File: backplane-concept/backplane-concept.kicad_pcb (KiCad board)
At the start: 2 copper layers, 60 x 91.8 mm, 2 parts

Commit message: Backplane Ideas
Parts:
- added J3: PCIE_8x_Labeled, !footprints:9-1734774-5, F.Cu at (60.0, 60.0)
- added J4: PCIE_8x_Labeled, !footprints:9-1734774-5, F.Cu at (60.0, 40.0)
- added J5: CONN_MINI, !footprints:10018784-10200TLF, F.Cu at (60.0, 100.0)
- added J6: CONN_MINI, !footprints:10018784-10200TLF, F.Cu at (60.0, 120.0)
- added J7: CONN_MINI, !footprints:10018784-10200TLF, F.Cu at (60.0, 140.0)
- added J8: CONN_MINI, !footprints:10018784-10200TLF, F.Cu at (60.0, 160.0)
- added U1: PRIMARY, !footprints:SPARKFUN_SEN-13879, F.Cu at (130.0, 83.0)
- added U2: SECONDARY, !footprints:SPARKFUN_SEN-13879, F.Cu at (130.0, 59.0)
- added U3: NAU7802SGI, !footprints:NAU7802SGI, F.Cu at (122.0, 100.0)
- added U5: ESP32-PICO-D4, Package_DFN_QFN:QFN-48-1EP_7x7mm_P0.5mm_EP5.3x5.3mm, F.Cu at (98.7, 161.7)
- J1: value ~ -> 6473427-1; footprint !footprints:9-1734774-5 -> !footprints:64734271
- J2: value ~ -> PCIE_8x_Labeled
- moved J1 112.2 mm to (117.2, 163.2), turned to 90 degrees
- moved J2 43.7 mm to (60.0, 80.0)
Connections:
- J1 pad A1: 5V -> +5V
- J1 pad A10: GND -> +5V
- J1 pad A11: GND -> ENCA_P
- J1 pad A12: ENGHALL1 -> ~ENCA_P
- J1 pad A13: DIR2 -> ENCB_P
- J1 pad A14: DIR1 -> ~ENCB_P
- J1 pad A15: PWM2 -> ENCI_P
- J1 pad A16: PWM1 -> ~ENCI_P
- J1 pad A18: SPARK -> +5V
- J1 pad A19: RRHALL -> ENCA_S
- J1 pad A2: 5V -> HALL1_P
- J1 pad A20: ENGHALL2 -> ~ENCA_S
- J1 pad A21: GND -> ENCB_S
- J1 pad A22: PLOADC1 -> ~ENCB_S
- J1 pad A23: PLOADC2 -> ENCI_S
- J1 pad A24: PLDCLK -> ~ENCI_S
- J1 pad A25: PLDDAT -> GND
- J1 pad A26: SLOADC1 -> +5V
- J1 pad A27: SLOADC2 -> HALL1_S
- J1 pad A28: SLDCLK -> HALL2_S
- J1 pad A29: SLDDAT -> HALL3_S
- J1 pad A3: 5V -> HALL2_P
- J1 pad A30: PENC_A -> GND
- J1 pad A31: ~PENC_A -> THERM_S
- J1 pad A32: PENC_B -> MOT1_S
- J1 pad A33: ~PENC_B -> MOT2_S
- J1 pad A34: SENC_A -> MOT3_S
- J1 pad A4: 3.3V -> HALL3_P
- J1 pad A5: 3.3V -> GND
- J1 pad A6: 3.3V -> THERM_P
- J1 pad A7: 8.4V -> MOT1_P
- J1 pad A8: 8.4V -> MOT2_P
- J1 pad A9: GND -> MOT3_P
- J1 pad B1: 5V -> GND
- J1 pad B10: GND -> +3V3
- J1 pad B12: CAN_H -> GND
- J1 pad B13: CAN_L -> THERM_A1_CASE
- J1 pad B14: GND -> THERM_A2_CASE
- J1 pad B15: I2C_DATA -> GND
- J1 pad B16: I2C_CLK -> IN+_P
- J1 pad B17: GND -> IN-_P
- J1 pad B18: TX1 -> AVDD_S
- J1 pad B19: RX1 -> GND
- J1 pad B2: 5V -> GND
- J1 pad B20: TX2 -> IN+_S
- J1 pad B21: RX2 -> IN-_S
- J1 pad B22: TX3 -> AVDD_S
- J1 pad B23: RX3 -> GND
- J1 pad B24: TX4 -> GND
- J1 pad B25: RX4 -> +3V3
- J1 pad B26: TX5 -> +3V3
- J1 pad B3: 5V -> HALL_ENG1
- J1 pad B4: 3.3V -> HALL_ENG2
- J1 pad B5: 3.3V -> +8V
- J1 pad B6: 3.3V -> +8V
- J1 pad B7: 8.4V -> GND
- J1 pad B8: 8.4V -> I2C1_ECVT_EXT_SDA
- J1 pad B9: GND -> I2C1_ECVT_EXT_SCL
- J2 pad A1: 5V -> +5V
- J2 pad A12: ENGHALL1 -> DAQ_TX0_ECVT_RX0
- J2 pad A13: DIR2 -> DAQ_RX0_ECVT_TX0
- J2 pad A14: DIR1 -> DAQ_TX1_DATA
- J2 pad A15: PWM2 -> GND
- J2 pad A16: PWM1 -> I2C1_DAQ_SDA
- J2 pad A17: GND -> I2C1_DAQ_SCL
- J2 pad A18: SPARK -> GND
- J2 pad A19: RRHALL -> unconnected-(J2-PadA19)
- J2 pad A2: 5V -> +5V
- J2 pad A20: ENGHALL2 -> unconnected-(J2-PadA20)
- J2 pad A21: GND -> unconnected-(J2-PadA21)
- J2 pad A22: PLOADC1 -> unconnected-(J2-PadA22)
- J2 pad A23: PLOADC2 -> unconnected-(J2-PadA23)
- J2 pad A24: PLDCLK -> unconnected-(J2-PadA24)
- J2 pad A25: PLDDAT -> unconnected-(J2-PadA25)
- J2 pad A26: SLOADC1 -> unconnected-(J2-PadA26)
- J2 pad A27: SLOADC2 -> unconnected-(J2-PadA27)
- J2 pad A28: SLDCLK -> GND
- J2 pad A29: SLDDAT -> ENCA_P
- J2 pad A3: 5V -> +5V
- J2 pad A30: PENC_A -> ~ENCA_P
- J2 pad A31: ~PENC_A -> ENCB_P
- J2 pad A32: PENC_B -> ~ENCB_P
- J2 pad A33: ~PENC_B -> ENCI_P
- J2 pad A34: SENC_A -> ~ENCI_P
- J2 pad A35: ~SENC_A -> GND
- J2 pad A36: SENC_B -> ENCA_S
- J2 pad A37: ~SENC_B -> ~ENCA_S
- J2 pad A38: GND -> ENCB_S
- J2 pad A39: DIG_OUT -> ~ENCB_S
- J2 pad A4: 3.3V -> +3V3
- J2 pad A40: N_A -> ENCI_S
- J2 pad A41: IR_TEENSY -> ~ENCI_S
- J2 pad A42: IR_AMP -> SPARK
- J2 pad A43: unconnected-(J2-PadA43) -> GND
- J2 pad A44: unconnected-(J2-PadA44) -> THERM_P
- J2 pad A45: GND -> THERM_S
- J2 pad A46: TEMP4 -> THERM_A1_CASE
- J2 pad A47: TEMP3 -> THERM_A2_CASE
- J2 pad A48: TEMP2 -> THERM_A3
- J2 pad A49: TEMP1 -> THERM_A4
- J2 pad A5: 3.3V -> +3V3
- J2 pad A6: 3.3V -> +3V3
- J2 pad A7: 8.4V -> +8V
- J2 pad A8: 8.4V -> +8V
- J2 pad B1: 5V -> +5V
- J2 pad B14: GND -> I2C0_DAQ_SDA
- J2 pad B15: I2C_DATA -> I2C0_DAQ_SCL
- J2 pad B16: I2C_CLK -> I2C0_ECVT_SDA
- J2 pad B17: GND -> I2C0_ECVT_SCL
- J2 pad B18: TX1 -> GND
- J2 pad B19: RX1 -> unconnected-(J2-PadB19)
- J2 pad B2: 5V -> +5V
- J2 pad B20: TX2 -> unconnected-(J2-PadB20)
- J2 pad B21: RX2 -> unconnected-(J2-PadB21)
- J2 pad B22: TX3 -> unconnected-(J2-PadB22)
- J2 pad B23: RX3 -> unconnected-(J2-PadB23)
- J2 pad B24: TX4 -> unconnected-(J2-PadB24)
- J2 pad B25: RX4 -> unconnected-(J2-PadB25)
- J2 pad B26: TX5 -> unconnected-(J2-PadB26)
- J2 pad B27: RX5 -> unconnected-(J2-PadB27)
- J2 pad B28: GND -> LOADC_CLK_P
- J2 pad B29: CIPO -> LOADC_DAT_P
- J2 pad B3: 5V -> +5V
- J2 pad B30: COPI -> LOADC_CLK_P
- J2 pad B31: SCLK -> LOADC_DAT_S
- J2 pad B32: CS1 -> GND
- J2 pad B33: CS2 -> HALL_ENG1
- J2 pad B34: CS3 -> HALL_RW
- J2 pad B35: CS4 -> PWM_P
- J2 pad B36: CS5 -> DIR_P
- J2 pad B37: CS6 -> PWM_S
- J2 pad B38: unconnected-(J2-PadB38) -> DIR_S
- J2 pad B39: unconnected-(J2-PadB39) -> I2C1_ECVT_EXT_SDA
- J2 pad B4: 3.3V -> +3V3
- J2 pad B40: unconnected-(J2-PadB40) -> I2C1_ECVT_EXT_SCL
- J2 pad B41: unconnected-(J2-PadB41) -> HALL_ENG2
- J2 pad B43: FRBPRESS -> GND
- J2 pad B44: RRBPRESS -> BP_FRONT
- J2 pad B45: RPOT1 -> BP_REAR
- J2 pad B46: RPOT2 -> RPOT1
- J2 pad B47: VOLT1 -> RPOT2
- J2 pad B48: VOLT2 -> Net-(J2-PadB48)
- J2 pad B49: VOLT3 -> Net-(J2-PadB49)
- J2 pad B5: 3.3V -> +3V3
- J2 pad B6: 3.3V -> +3V3
- J2 pad B7: 8.4V -> +8V
- J2 pad B8: 8.4V -> +8V
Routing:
- net GND: track 166.5 -> 452.8 mm, vias 0 -> 16
- net I2C0_ECVT_SCL: track 0.00 -> 127.0 mm, vias 0 -> 12
- net I2C0_DAQ_SCL: track 0.00 -> 127.0 mm, vias 0 -> 12
- net I2C0_ECVT_SDA: track 0.00 -> 123.8 mm, vias 0 -> 12
- net I2C0_DAQ_SDA: track 0.00 -> 123.8 mm, vias 0 -> 12
- net DAQ_RX0_ECVT_TX0: track 0.00 -> 122.8 mm
- net I2C1_DAQ_SCL: track 0.00 -> 122.8 mm
- net I2C1_DAQ_SDA: track 0.00 -> 122.7 mm
- net DAQ_TX1_DATA: track 0.00 -> 122.7 mm
- net DAQ_TX0_ECVT_RX0: track 0.00 -> 122.7 mm
- net LOADC_CLK_P: track 0.00 -> 82.5 mm, vias 0 -> 8
- net CAN_L: track 62.0 -> 127.0 mm, vias 0 -> 12
- net CAN_H: track 62.0 -> 123.8 mm, vias 0 -> 12
- net PWM_P: track 0.00 -> 42.5 mm, vias 0 -> 4
- net LOADC_DAT_S: track 0.00 -> 42.5 mm, vias 0 -> 4
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- added copper zone on B.Cu, net +3V3
- added copper zone on F.Cu, net +3V3
- added copper zone on B.Cu, net +5V
- added copper zone on F.Cu, net +5V
- added copper zone on B.Cu, net +8V
- added copper zone on F.Cu, net +8V
- removed copper zone on B.Cu, net 3.3V
- removed copper zone on F.Cu, net 3.3V
- removed copper zone on B.Cu, net 5V
- removed copper zone on F.Cu, net 5V
- removed copper zone on B.Cu, net 8.4V
- removed copper zone on F.Cu, net 8.4V
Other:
- board size 60 x 91.8 mm -> 90 x 140 mm

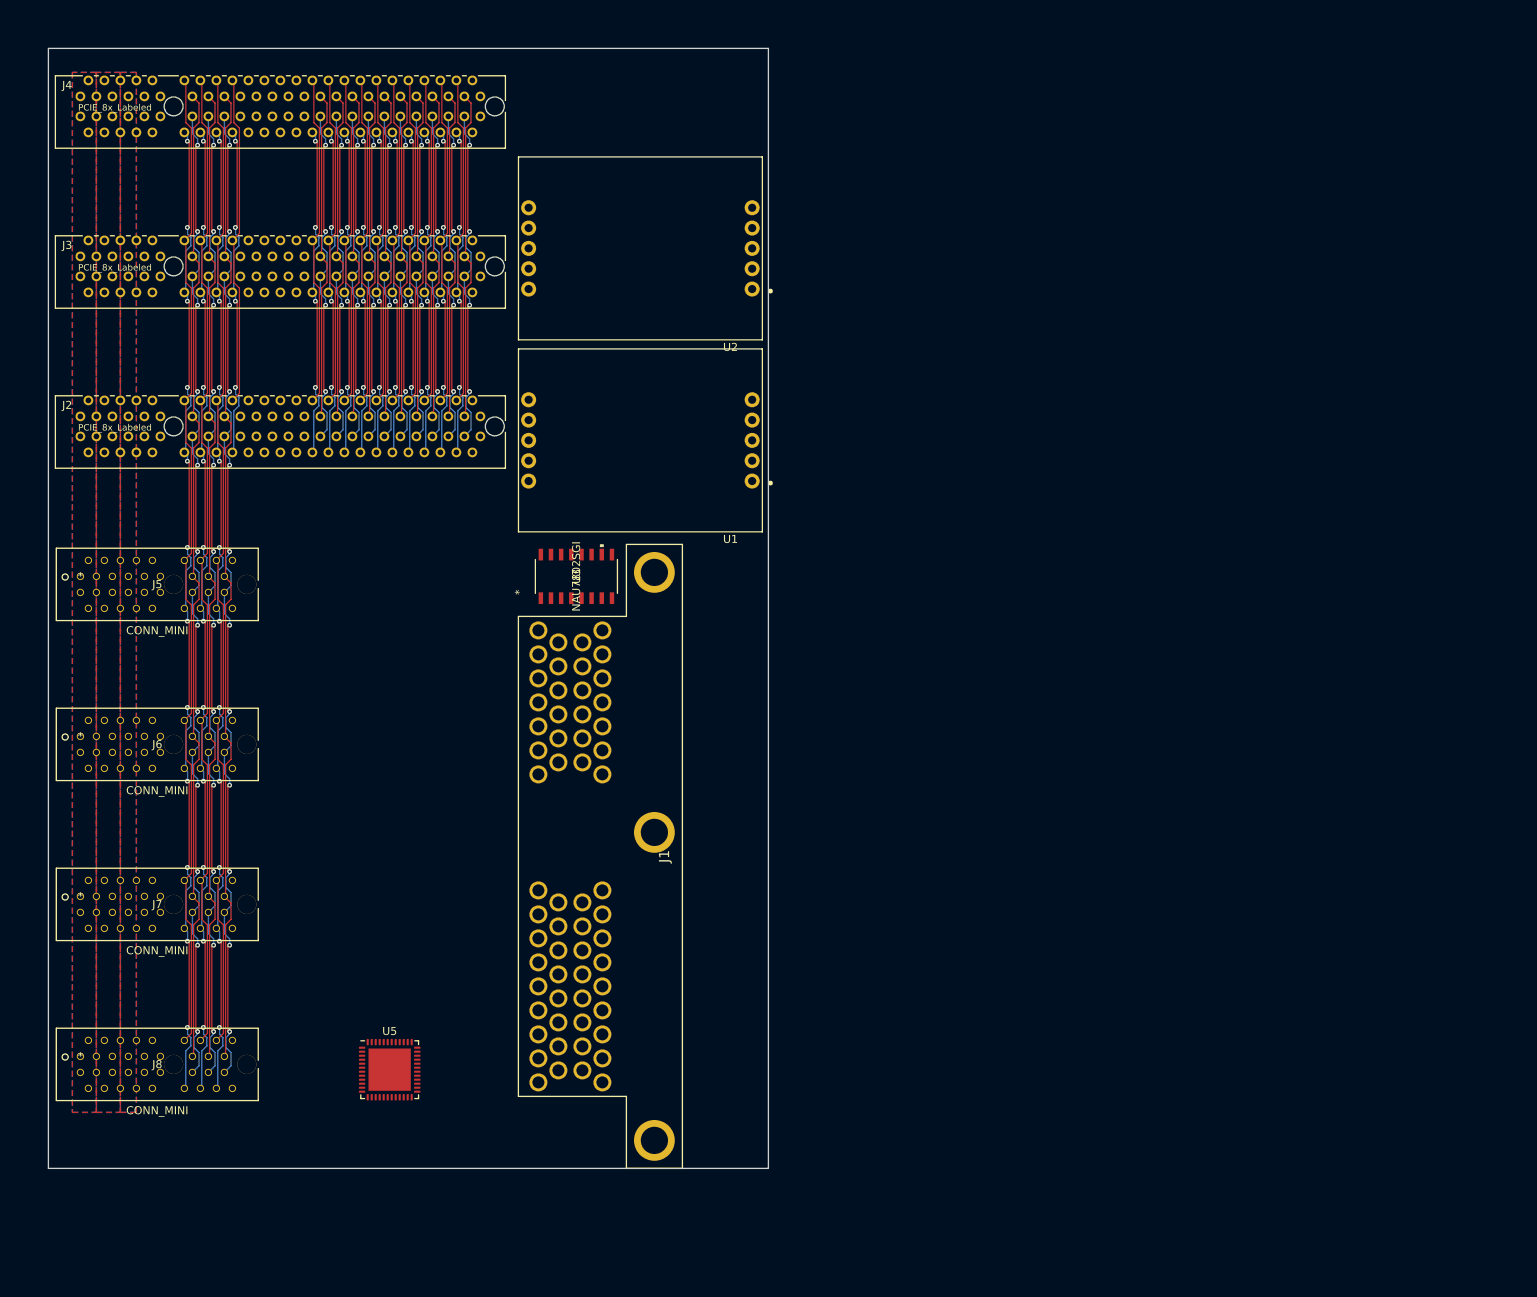
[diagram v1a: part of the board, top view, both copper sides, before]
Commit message: Design PSUs, route bucks
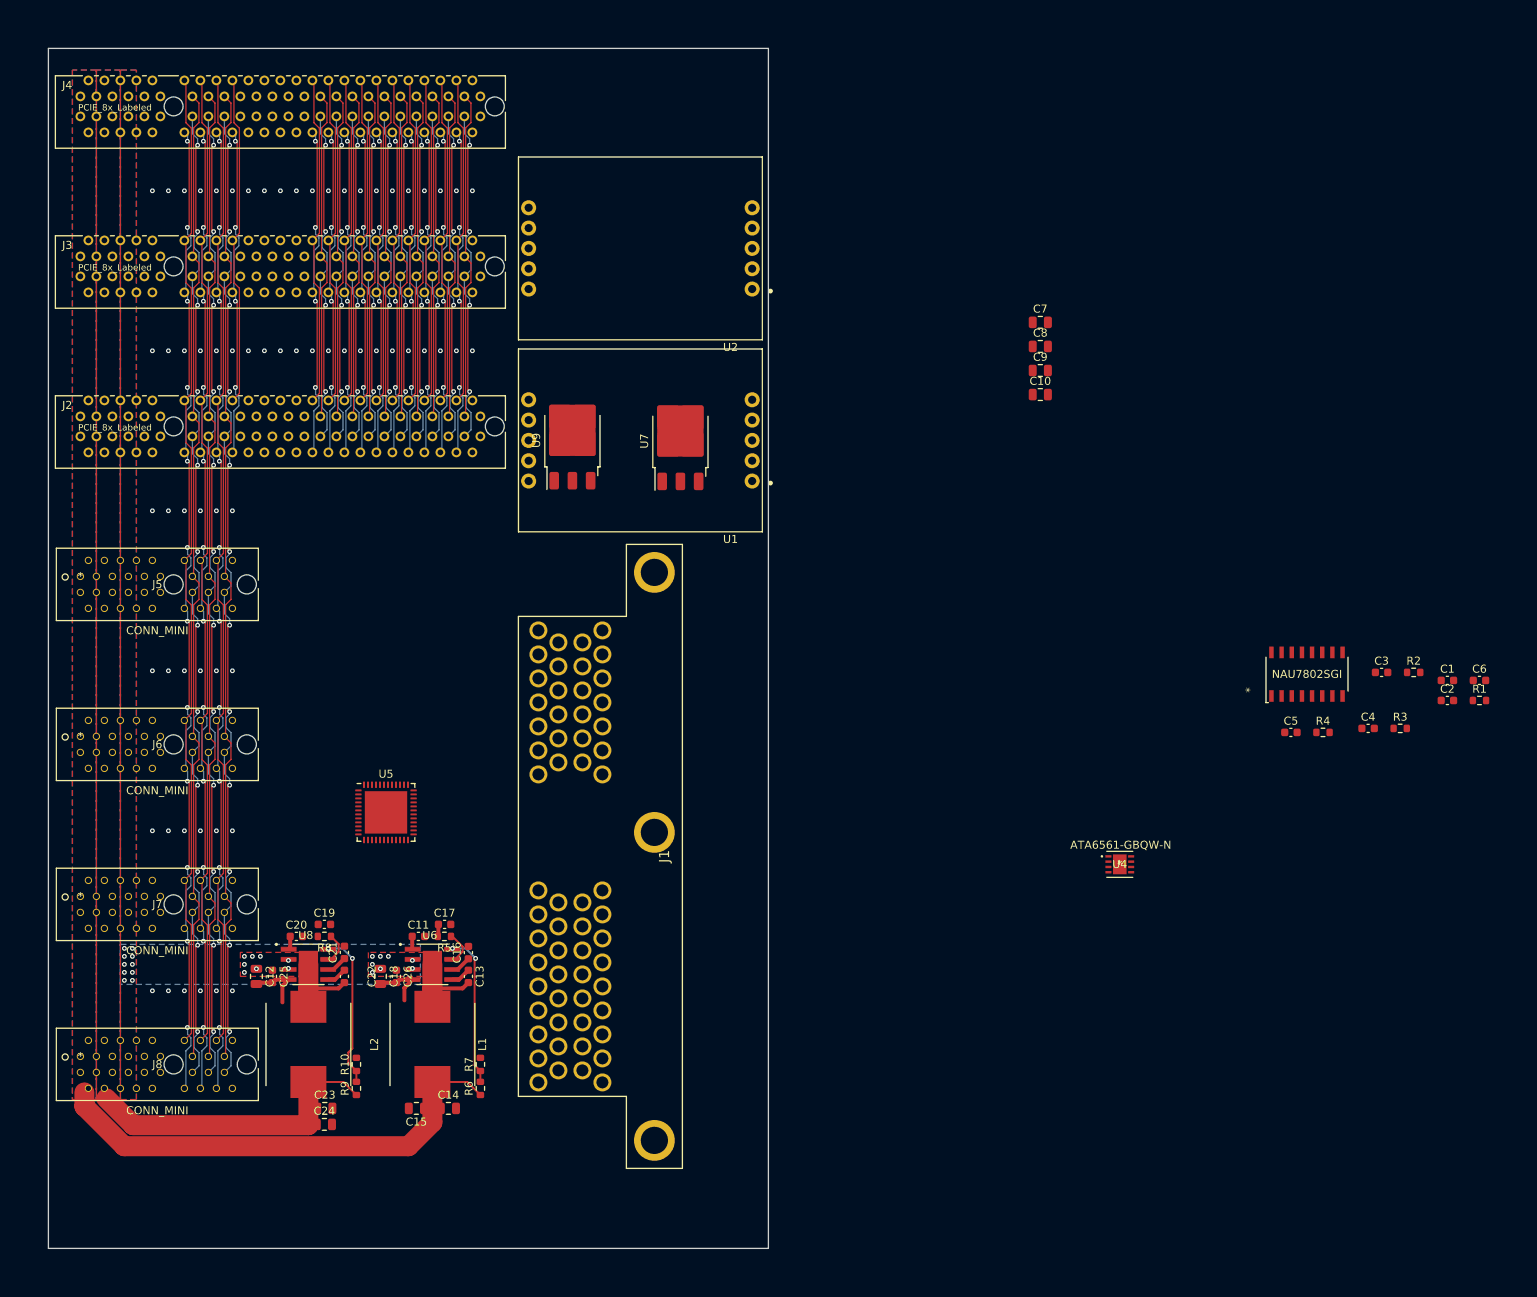
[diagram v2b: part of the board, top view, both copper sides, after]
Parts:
- added C1: 1uF, Capacitor_SMD:C_0603_1608Metric, F.Cu at (230.9, 113.0)
- added C10: 22uF, Capacitor_SMD:C_0805_2012Metric, F.Cu at (180.0, 77.3)
- added C11: 47nF, Capacitor_SMD:C_0603_1608Metric, F.Cu at (102.2, 145.0)
- added C12: 22uF, Capacitor_SMD:C_0805_2012Metric, F.Cu at (82.0, 150.0)
- added C13: 0.1uF, Capacitor_SMD:C_0603_1608Metric, F.Cu at (108.5, 150.0)
- added C14: 22uF, Capacitor_SMD:C_0805_2012Metric, F.Cu at (106.0, 166.5)
- added C15: 22uF, Capacitor_SMD:C_0805_2012Metric, F.Cu at (102.0, 166.5)
- added C16: 1uF, Capacitor_SMD:C_0603_1608Metric, F.Cu at (108.5, 147.0)
- added C17: 1.8nF, Capacitor_SMD:C_0603_1608Metric, F.Cu at (105.5, 143.5)
- added C18: 22uF, Capacitor_SMD:C_0805_2012Metric, F.Cu at (97.5, 150.0)
- added C19: 1.8nF, Capacitor_SMD:C_0603_1608Metric, F.Cu at (90.5, 143.5)
- added C2: 0.1uF, Capacitor_SMD:C_0603_1608Metric, F.Cu at (230.9, 115.5)
- added C20: 47nF, Capacitor_SMD:C_0603_1608Metric, F.Cu at (87.0, 145.0)
- added C21: 1uF, Capacitor_SMD:C_0603_1608Metric, F.Cu at (93.0, 147.0)
- added C22: 0.1uF, Capacitor_SMD:C_0603_1608Metric, F.Cu at (93.0, 150.0)
- added C23: 22uF, Capacitor_SMD:C_0805_2012Metric, F.Cu at (90.5, 166.5)
- added C24: 22uF, Capacitor_SMD:C_0805_2012Metric, F.Cu at (90.5, 168.5)
- added C25: 0.1uF, Capacitor_SMD:C_0603_1608Metric, F.Cu at (84.0, 150.0)
- added C26: 0.1uF, Capacitor_SMD:C_0603_1608Metric, F.Cu at (99.5, 150.0)
- added C3: 1uF, Capacitor_SMD:C_0603_1608Metric, F.Cu at (222.7, 112.0)
- added C4: 0.1uF, Capacitor_SMD:C_0603_1608Metric, F.Cu at (221.0, 119.0)
- added C5: 0.1uF, Capacitor_SMD:C_0603_1608Metric, F.Cu at (211.3, 119.5)
- added C6: 0.1uF, Capacitor_SMD:C_0603_1608Metric, F.Cu at (234.9, 113.0)
- added C7: 22uF, Capacitor_SMD:C_0805_2012Metric, F.Cu at (180.0, 68.2)
- added C8: 22uF, Capacitor_SMD:C_0805_2012Metric, F.Cu at (180.0, 71.3)
- added C9: 22uF, Capacitor_SMD:C_0805_2012Metric, F.Cu at (180.0, 74.3)
- added L1: 3.8uH, Inductor_SMD:L_Taiyo-Yuden_NR-10050_9.8x10.0mm_HandSoldering, F.Cu at (104.0, 158.5)
- added L2: 3.8uH, Inductor_SMD:L_Taiyo-Yuden_NR-10050_9.8x10.0mm_HandSoldering, F.Cu at (88.5, 158.5)
- added R1: 47, Resistor_SMD:R_0603_1608Metric, F.Cu at (234.9, 115.5)
- added R10: 15K, Resistor_SMD:R_0603_1608Metric, F.Cu at (94.5, 161.0)
- added R2: 47, Resistor_SMD:R_0603_1608Metric, F.Cu at (226.7, 112.0)
- added R3: 47, Resistor_SMD:R_0603_1608Metric, F.Cu at (225.0, 119.0)
- added R4: 47, Resistor_SMD:R_0603_1608Metric, F.Cu at (215.3, 119.5)
- added R5: 14.7K, Resistor_SMD:R_0603_1608Metric, F.Cu at (105.5, 145.0)
- added R6: 110K, Resistor_SMD:R_0603_1608Metric, F.Cu at (110.0, 164.0)
- added R7: 15K, Resistor_SMD:R_0603_1608Metric, F.Cu at (110.0, 161.0)
- added R8: 10K, Resistor_SMD:R_0603_1608Metric, F.Cu at (90.5, 145.0)
- added R9: 67.5K, Resistor_SMD:R_0603_1608Metric, F.Cu at (94.5, 164.0)
- added U4: ATA6561-GBQW-N, !footprints:ATA6561-GBQW-N, F.Cu at (189.9, 136.0)
- added U6: 5V Reg, !footprints:AOZ6605PI-1, F.Cu at (104.0, 148.5)
- added U7: AMS1117CD-5.0, Package_TO_SOT_SMD:TO-252-3_TabPin2, F.Cu at (135.0, 83.1)
- added U8: 3.3V Reg, !footprints:AOZ6605PI-1, F.Cu at (88.5, 148.5)
- added U9: AMS1117CD-3.3, Package_TO_SOT_SMD:TO-252-3_TabPin2, F.Cu at (121.5, 83.0)
- moved U3 92.1 mm to (213.3, 112.2)
- moved U5 32.2 mm to (98.2, 129.5)
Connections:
- J1 pad A1: +5V -> +5VA
- J1 pad A18: +5V -> +5VA
- J1 pad A26: +5V -> +5VA
- J1 pad B10: +3V3 -> +3.3VA
- J1 pad B25: +3V3 -> +3.3VA
- J1 pad B26: +3V3 -> +3.3VA
- U1 pad 10: +5V -> +5VA
- U1 pad 9: +3V3 -> +3.3VA
- U2 pad 9: +3V3 -> +3.3VA
- U3 pad 15: +3V3 -> +3.3VA
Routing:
- net +5V: track 0.00 -> 60.3 mm
- net +3V3: track 0.00 -> 38.7 mm
- net Net-(U8-FB): track 0.00 -> 19.6 mm, vias 0 -> 2
- net Net-(U6-FB): track 0.00 -> 19.2 mm, vias 0 -> 2
- net GND: track 452.8 -> 467.0 mm, vias 16 -> 82
- net Net-(U8-LX): track 0.00 -> 10.1 mm
- net Net-(U6-LX): track 0.00 -> 10.1 mm
- net Net-(U6-COMP): track 0.00 -> 3.79 mm
- net Net-(U8-COMP): track 0.00 -> 3.65 mm
- net Net-(U8-BST): track 0.00 -> 2.51 mm
- net Net-(U6-BST): track 0.00 -> 2.51 mm
- net Net-(U8-VCC): track 0.00 -> 1.92 mm
- net Net-(U6-VCC): track 0.00 -> 1.89 mm
- net Net-(U8-SS): track 0.00 -> 1.68 mm
- net Net-(U6-SS): track 0.00 -> 1.54 mm
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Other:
- board size 90 x 140 mm -> 90 x 150 mm
- board text added: "PSU Gen here"
- board text added: "PSU Interconnect here"
